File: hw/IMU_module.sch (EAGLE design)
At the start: 23 parts, among them J1 GROVE-4P-2.0-3470130P1, J2 GROVE-4P-2.0-3470130P1

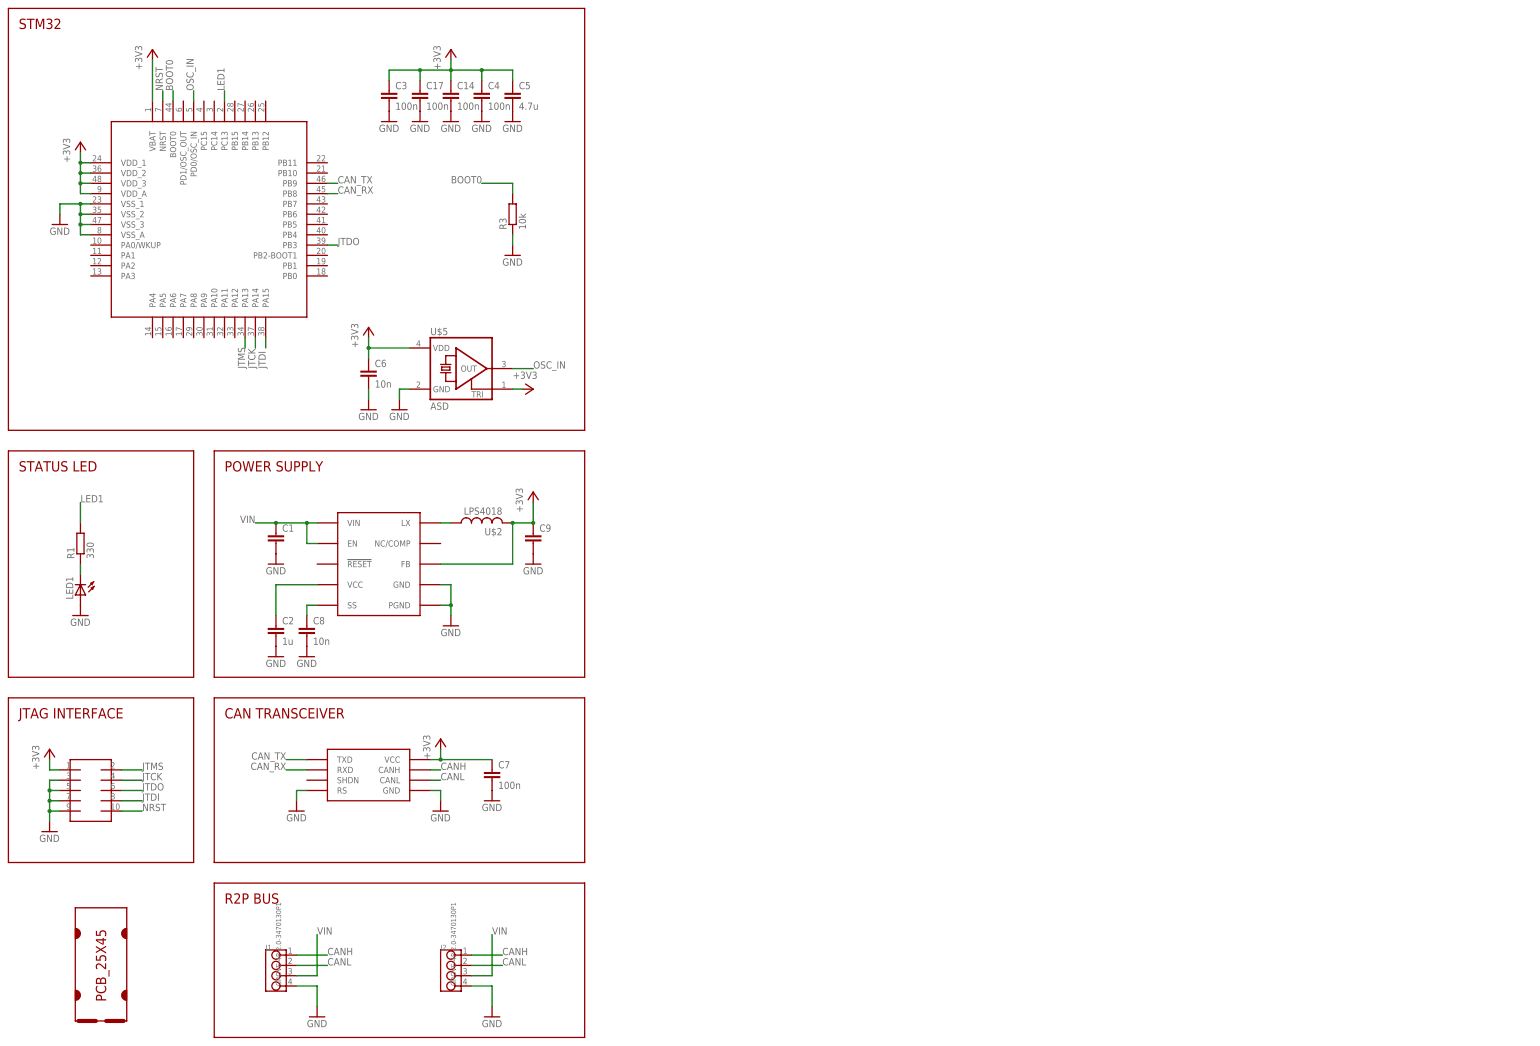
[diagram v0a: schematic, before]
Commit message: added MEMS datasheets to doc foder
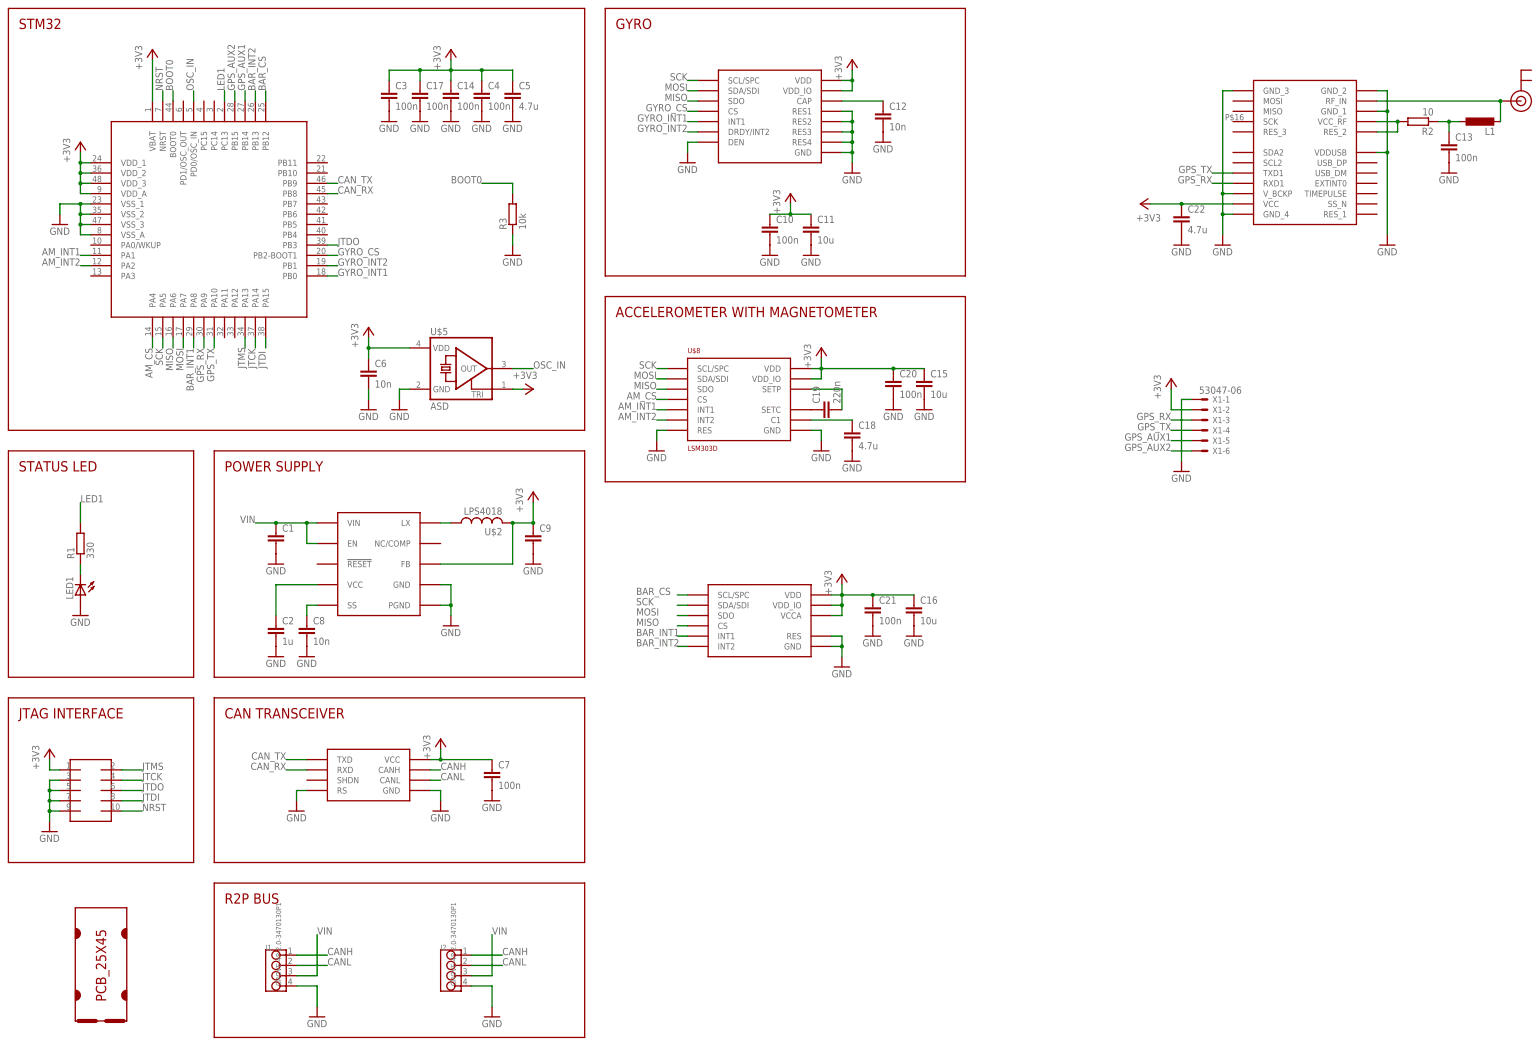
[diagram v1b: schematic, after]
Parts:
- added C10, C13, C20, C21: 100n, rcl:C-EUC0603
- added C11, C15, C16: 10u, rcl:C-EUC0805
- added C12: 10n, rcl:C-EUC0603
- added C18, C22: 4.7u, rcl:C-EUC0805
- added C19: 220n, rcl:C-EUC0603
- added L1: (no value), rcl:L-EUL2012C
- added R2: 10, rcl:R-EU_R0603
- added U$10: NEO-6, u-blox:NEO-6
- added U$11: U.FL, SparkFun:U.FL
- added U$7: L3GD20H, st:L3GD20H
- added U$8: LSM303D, st:LSM303D
- added U$9: LPS331AP, st:LPS331AP
- added X1: 53047-06, con-molex:53047-06
- U$6: value STM32F103CX -> STM32F103CXTX; device st:STM32F103CX -> st:STM32F103CXTX
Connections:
- new net AM_CS: U$6.PA4, U$8.CS
- new net AM_INT1: U$6.PA1, U$8.INT1
- new net AM_INT2: U$6.PA2, U$8.INT2
- new net BAR_CS: U$6.PB12, U$9.SCL/SPC
- new net BAR_INT1: U$6.PA8, U$9.INT1
- new net BAR_INT2: U$6.PB13, U$9.INT2
- new net GPS_AUX1: U$6.PB14, X1-5.S
- new net GPS_AUX2: U$6.PB15, X1-6.S
- new net GPS_RX: U$10.RXD1, U$6.PA9, X1-3.S
- new net GPS_TX: U$10.TXD1, U$6.PA10, X1-4.S
- new net GYRO_CS: U$6.PB2-BOOT1, U$7.CS
- new net GYRO_INT1: U$6.PB0, U$7.INT1
- new net GYRO_INT2: U$6.PB1, U$7.DRDY/INT2
- new net MISO: U$6.PA6, U$7.SDO, U$8.SDO, U$9.CS
- new net MOSI: U$6.PA7, U$7.SDA/SDI, U$8.SDA/SDI, U$9.SDO
- new net N$10: L1.2, U$10.RF_IN, U$11.SIGNAL
- new net N$11: C13.1, L1.1, R2.1
- new net N$12: R2.2, U$10.RES_2, U$10.VCC_RF
- new net N$3: C12.1, U$7.CAP
- new net N$5: C18.1, U$8.C1
- new net N$6: C19.1, U$8.SETC
- new net N$9: C19.2, U$8.SETP
- new net SCK: U$6.PA5, U$7.SCL/SPC, U$8.SCL/SPC, U$9.SDA/SDI
- net +3V3: now also C10.1, C11.1, C15.1, C16.1, C20.1, C21.1, C22.1, U$10.VCC, U$7.VDD, U$7.VDD_IO, U$8.VDD, U$8.VDD_IO, U$9.VCCA, U$9.VDD, U$9.VDD_IO, X1-2.S
- net GND: now also C10.2, C11.2, C12.2, C13.2, C15.2, C16.2, C18.2, C20.2, C21.2, C22.2, U$10.GND_1, U$10.GND_2, U$10.GND_3, U$10.GND_4, U$10.VDDUSB, U$10.V_BCKP, U$7.DEN, U$7.GND, U$7.RES1, U$7.RES2, U$7.RES3, U$7.RES4, U$8.GND, U$8.RES, U$9.GND, U$9.RES, X1-1.S
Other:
- note added: "ACCELEROMETER WITH MAGNETOMETER"
- note added: "GYRO"

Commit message: added TIMEPULSE and INT0 signals
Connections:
- net GPS_AUX1: now also U$10.TIMEPULSE
- net GPS_AUX2: now also U$10.EXTINT0
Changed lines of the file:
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@@
 <label x="63.5" y="238.76" size="1.778" layer="95" rot="R90"/>
+</segment>
+<segment>
+<pinref part="U$10" gate="G$1" pin="TIMEPULSE"/>
+<wire x1="342.9" y1="213.36" x2="347.98" y2="213.36" width="0.1524" layer="91"/>
+<label x="347.98" y="213.36" size="1.778" layer="95"/>
 </segment>
 </net>
@@
 <label x="60.96" y="238.76" size="1.778" layer="95" rot="R90"/>
 </segment>
+<segment>
+<pinref part="U$10" gate="G$1" pin="EXTINT0"/>
+<wire x1="342.9" y1="215.9" x2="347.98" y2="215.9" width="0.1524" layer="91"/>
+<label x="347.98" y="215.9" size="1.778" layer="95"/>
+</segment>
 </net>

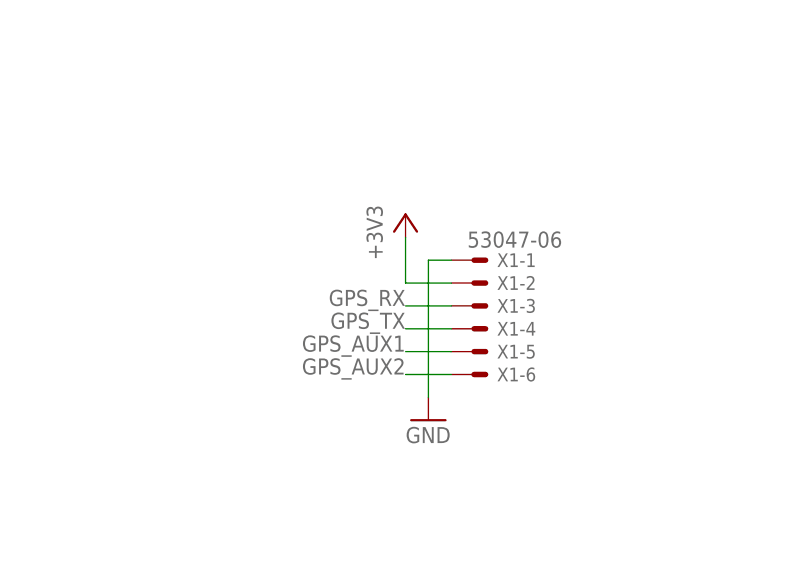
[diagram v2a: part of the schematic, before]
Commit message: updated GPS connector to have Vcc on pin 1
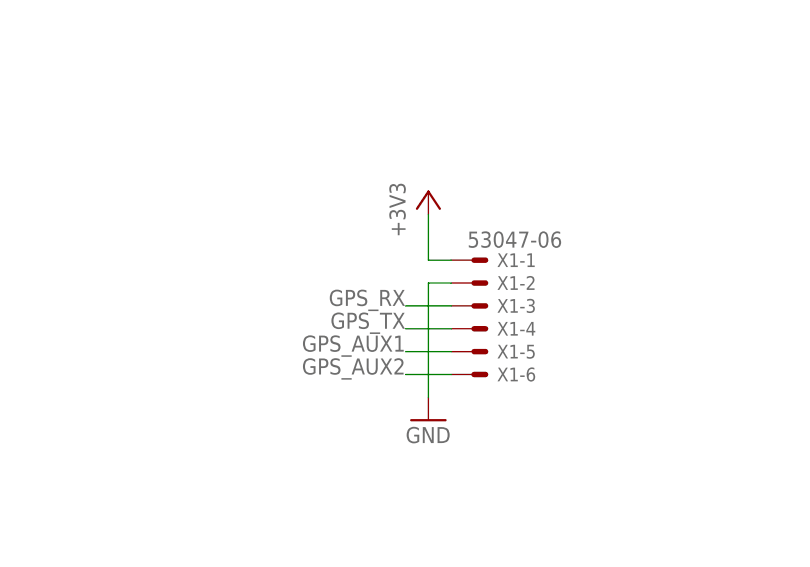
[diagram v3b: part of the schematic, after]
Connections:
- net +3V3: now also X1-1.S; no longer X1-2.S
- net GND: now also X1-2.S; no longer X1-1.S
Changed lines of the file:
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@@
 <instance part="X1" gate="-5" x="299.72" y="152.4"/>
 <instance part="X1" gate="-6" x="299.72" y="149.86"/>
-<instance part="+3V14" gate="G$1" x="292.1" y="167.64"/>
+<instance part="+3V14" gate="G$1" x="294.64" y="170.18"/>
 <instance part="GND35" gate="1" x="294.64" y="144.78"/>
 <instance part="+3V8" gate="G$1" x="198.12" y="213.36"/>
@@
 </segment>
 <segment>
-<pinref part="X1" gate="-1" pin="S"/>
-<wire x1="297.18" y1="162.56" x2="294.64" y2="162.56" width="0.1524" layer="91"/>
-<wire x1="294.64" y1="162.56" x2="294.64" y2="147.32" width="0.1524" layer="91"/>
+<wire x1="294.64" y1="160.02" x2="294.64" y2="147.32" width="0.1524" layer="91"/>
 <pinref part="GND35" gate="1" pin="GND"/>
+<pinref part="X1" gate="-2" pin="S"/>
+<wire x1="297.18" y1="160.02" x2="294.64" y2="160.02" width="0.1524" layer="91"/>
 </segment>
 <segment>
@@
 </segment>
 <segment>
-<pinref part="X1" gate="-2" pin="S"/>
-<wire x1="297.18" y1="160.02" x2="292.1" y2="160.02" width="0.1524" layer="91"/>
-<wire x1="292.1" y1="160.02" x2="292.1" y2="165.1" width="0.1524" layer="91"/>
+<wire x1="294.64" y1="162.56" x2="294.64" y2="167.64" width="0.1524" layer="91"/>
 <pinref part="+3V14" gate="G$1" pin="+3V3"/>
-</segment>
-<segment>
+<pinref part="X1" gate="-1" pin="S"/>
+<wire x1="297.18" y1="162.56" x2="294.64" y2="162.56" width="0.1524" layer="91"/>
+</segment>
+<segment>
